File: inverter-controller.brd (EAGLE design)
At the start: 66 x 27.6 mm, 187 parts, among them IC1 STM32F334C8T6, IC2 SY7152ABC, IC3 LMV358MMX, IC4 LMV358MMX, IC5 SY7152ABC, J1 621006245821, J2 61300211121, K1 FINDER_34.51.7.024.0010FINDER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, K2 FINDER_34.51.7.024.0010FINDER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, K3 FINDER_34.51.7.024.0010FINDER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, U1 DIODES_AP3015KTR-G1DIODES_AP3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, X1 0289-9066**15EDGVC-3.81-02P-14, X2 0289-9066**15EDGVC-3.81-02P-14, X3 0289-9066**15EDGVC-3.81-02P-14, X4 0289-9066**15EDGVC-3.81-02P-14, X5 1365-10, X6 1365-16, X7 1365-10, X8 1365-10, Y1 NX2016SA-32M

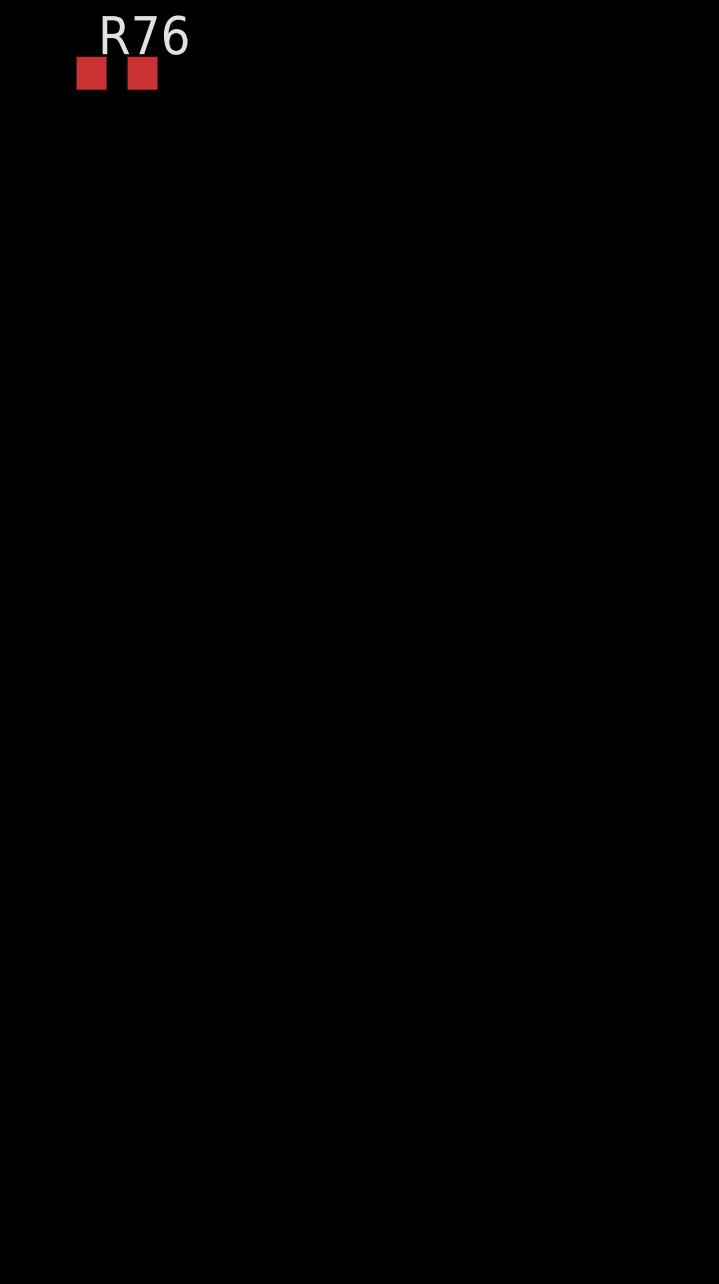
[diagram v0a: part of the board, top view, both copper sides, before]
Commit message: Relay soketleri eklendi.
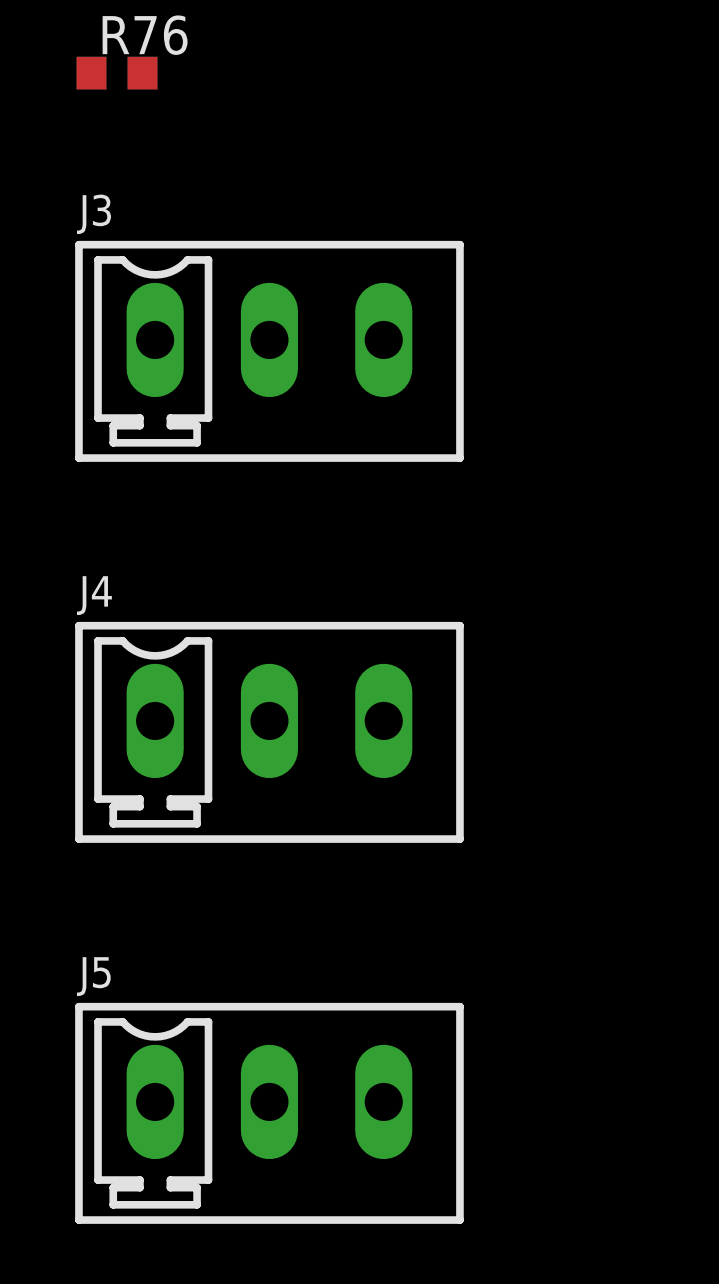
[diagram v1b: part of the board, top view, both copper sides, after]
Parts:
- added J3, J4, J5: MCV3, con-phoenix-381:MCV3
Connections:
- new net NC: J3.2, J4.2, J5.2
- new net NO: J3.3, J4.3, J5.3
- net COM1: now also J3.1
- net COM2: now also J4.1
- net COM3: now also J5.1
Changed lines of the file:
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@@
 <attribute name="VALUE" x="-126.365" y="-53.975" size="1.27" layer="27"/>
+</element>
+<element name="J3" library="con-phoenix-381" library_urn="urn:adsk.eagle:library:27486877" package="MCV3" package3d_urn="urn:adsk.eagle:package:27487037/1" value="MCV3" x="-120.65" y="-60.96" smashed="yes">
+<attribute name="NAME" x="-127" y="-57.15" size="1.016" layer="25" ratio="18"/>
+<attribute name="VALUE" x="-127" y="-66.929" size="0.8128" layer="27" ratio="10"/>
+</element>
+<element name="J4" library="con-phoenix-381" library_urn="urn:adsk.eagle:library:27486877" package="MCV3" package3d_urn="urn:adsk.eagle:package:27487037/1" value="MCV3" x="-120.65" y="-73.66" smashed="yes">
+<attribute name="NAME" x="-127" y="-69.85" size="1.016" layer="25" ratio="18"/>
+<attribute name="VALUE" x="-127" y="-79.629" size="0.8128" layer="27" ratio="10"/>
+</element>
+<element name="J5" library="con-phoenix-381" library_urn="urn:adsk.eagle:library:27486877" package="MCV3" package3d_urn="urn:adsk.eagle:package:27487037/1" value="MCV3" x="-120.65" y="-86.36" smashed="yes">
+<attribute name="NAME" x="-127" y="-82.55" size="1.016" layer="25" ratio="18"/>
+<attribute name="VALUE" x="-127" y="-92.329" size="0.8128" layer="27" ratio="10"/>
 </element>
 </elements>
@@
 <signal name="COM1">
 <contactref element="K1" pad="11"/>
+<contactref element="J3" pad="1"/>
+<wire x1="57.9" y1="60.89" x2="-124.46" y2="-60.96" width="0" layer="19" extent="1-1"/>
 </signal>
 <signal name="NO2">
@@
 <signal name="COM2">
 <contactref element="K2" pad="11"/>
+<contactref element="J4" pad="1"/>
+<wire x1="57.9" y1="50.73" x2="-124.46" y2="-73.66" width="0" layer="19" extent="1-1"/>
 </signal>
 <signal name="COM3">
 <contactref element="K3" pad="11"/>
+<contactref element="J5" pad="1"/>
+<wire x1="57.9" y1="40.57" x2="-124.46" y2="-86.36" width="0" layer="19" extent="1-1"/>
 </signal>
 <signal name="NO3">
@@
 <wire x1="18.76" y1="37.672" x2="-105.41" y2="-36.42" width="0" layer="19" extent="1-16"/>
 </signal>
+<signal name="NC">
+<contactref element="J3" pad="2"/>
+<contactref element="J4" pad="2"/>
+<contactref element="J5" pad="2"/>
+<wire x1="-120.65" y1="-73.66" x2="-120.65" y2="-86.36" width="0" layer="19" extent="1-1"/>
+<wire x1="-120.65" y1="-60.96" x2="-120.65" y2="-73.66" width="0" layer="19" extent="1-1"/>
+</signal>
+<signal name="NO">
+<contactref element="J3" pad="3"/>
+<contactref element="J4" pad="3"/>
+<contactref element="J5" pad="3"/>
+<wire x1="-116.84" y1="-73.66" x2="-116.84" y2="-86.36" width="0" layer="19" extent="1-1"/>
+<wire x1="-116.84" y1="-60.96" x2="-116.84" y2="-73.66" width="0" layer="19" extent="1-1"/>
+</signal>
 </signals>

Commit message: Mekanik kistaslar belirlendi.
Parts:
- removed D7: (no value), diode:SOD80C
- removed J5: MCV3, con-phoenix-381:MCV3
- removed K3: FINDER_34.51.7.024.0010FINDER_34.51.7.024.0010_0_0, Finder - 34.51.7.024.0010:FINDER_34.51.7.024.0010_0
- removed LED3: (no value), adafruit:CHIPLED_0805
- removed Q3: (no value), adafruit:SOT23
- removed R40: (no value), rcl:R0603
- removed R41: 22R, rcl:R0603
- removed R44: 470R, rcl:R0603
- moved J4 217.1 mm to (54.7, 54.2), turned to 180 degrees
- moved J3 203.2 mm to (62.4, 27.2)
- moved X6 169.9 mm to (54.5, 40.9)
- moved X2 146.7 mm to (51.2, 27.2), turned to 180 degrees
- moved X4 127.0 mm to (32.8, 27.2), turned to 180 degrees
- moved C4 112.1 mm to (27.9, 38.3), flipped to the bottom, turned to 90 degrees
- moved C5 102.3 mm to (29.1, 38.3), flipped to the bottom, turned to 90 degrees
- moved C3 100.7 mm to (29.0, 35.1), flipped to the bottom, turned to 270 degrees
- moved X3 93.5 mm to (42.0, 27.2), turned to 180 degrees
- moved X1 77.3 mm to (23.6, 27.2), turned to 180 degrees
- moved K1 20.0 mm to (33.7, 49.3)
- moved J1 19.6 mm to (45.7, 36.9)
- moved IC1 19.6 mm to (35.5, 36.9)
- moved K2 18.3 mm to (33.6, 55.7)
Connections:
- removed net COM3: J5.1, K3.11
- removed net N$28: Q3.1, R40.2, R41.1
- removed net N$31: D7.A, K3.A1, LED3.C, Q3.3
- removed net N$33: LED3.A, R44.1
- removed net NC3: K3.12
- removed net NO3: K3.14
- net GND: no longer Q3.2, R40.1
- net NC: no longer J5.2
- net NO: no longer J5.3
- net RELAY3: no longer R41.2
- net VDD: no longer D7.C, K3.A2, R44.2
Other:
- board size 66 x 27.6 mm -> 52 x 37.6 mm

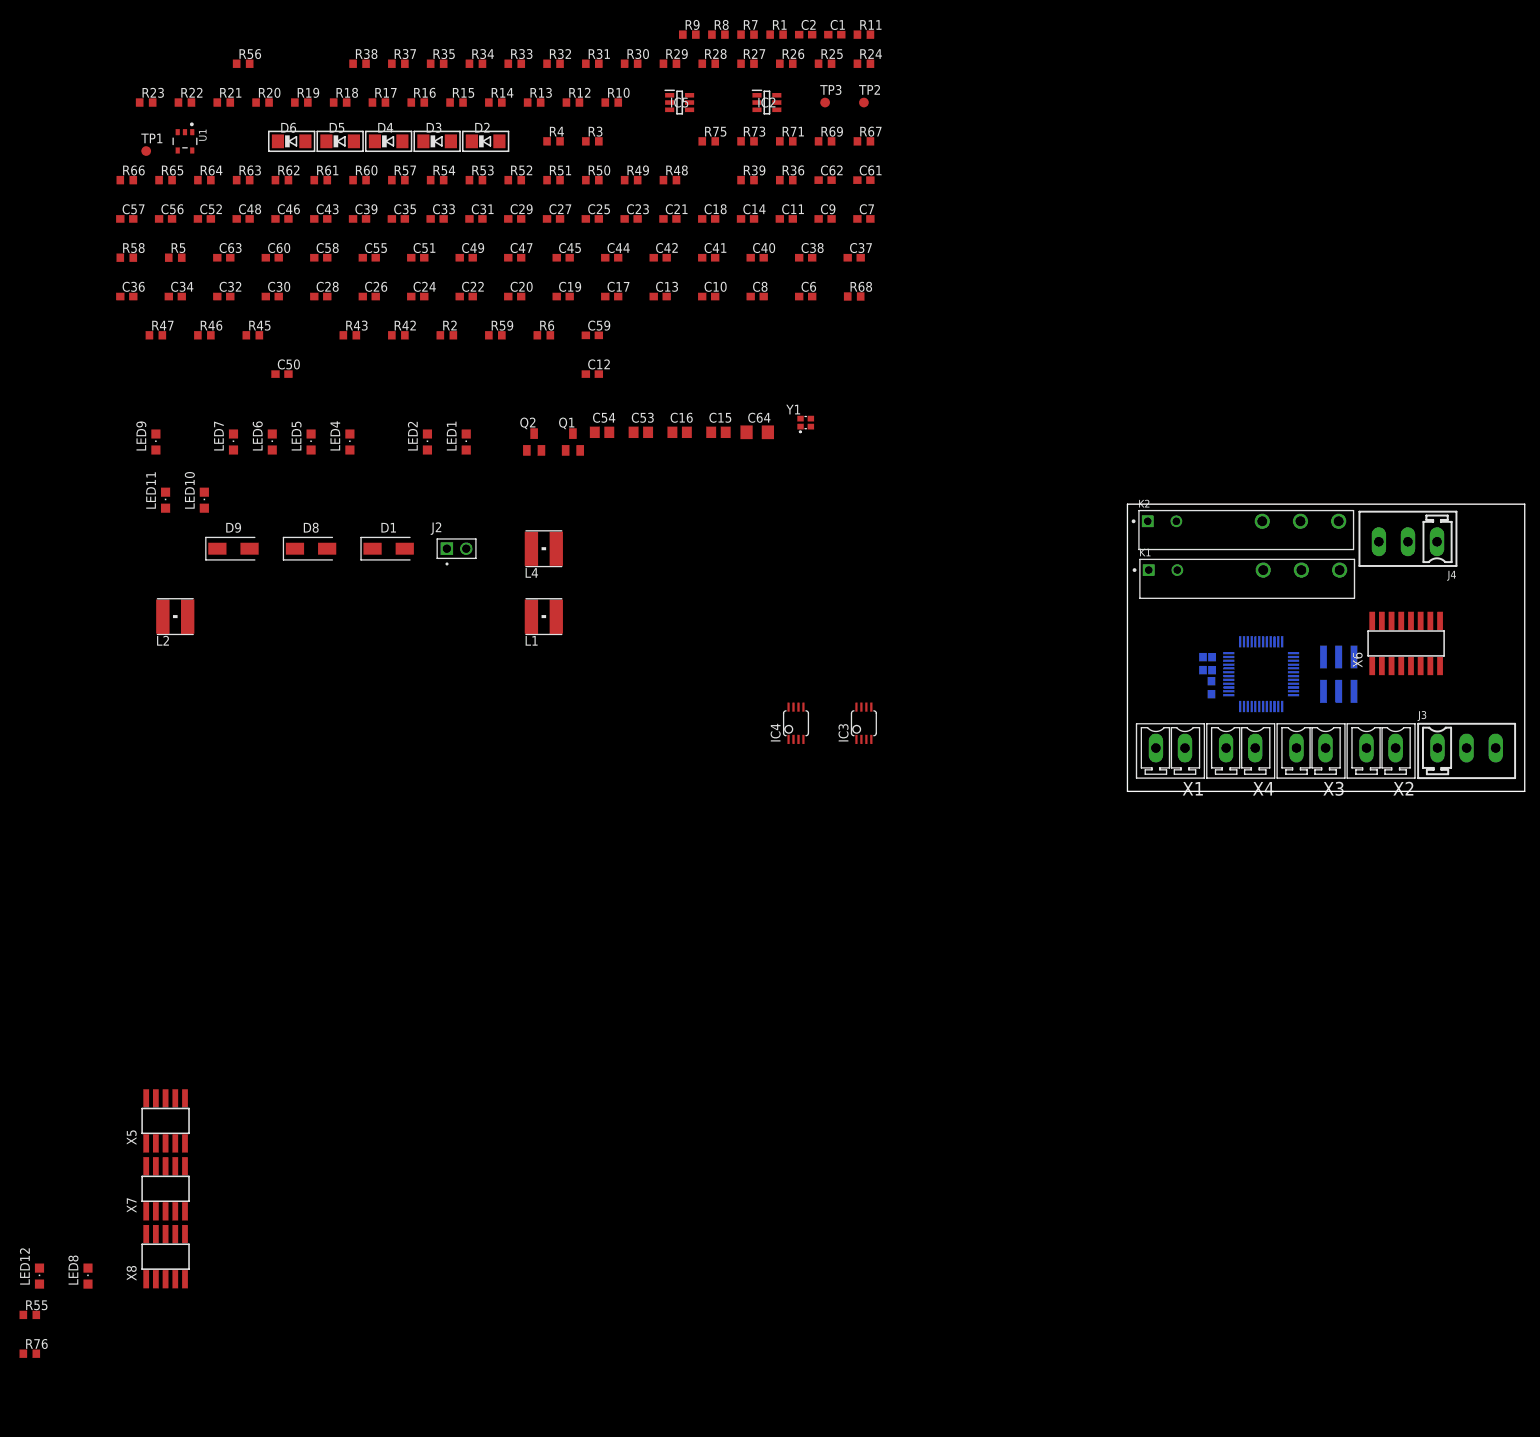
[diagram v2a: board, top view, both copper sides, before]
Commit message: Mini kart tasarimi icin sadelestirildi.
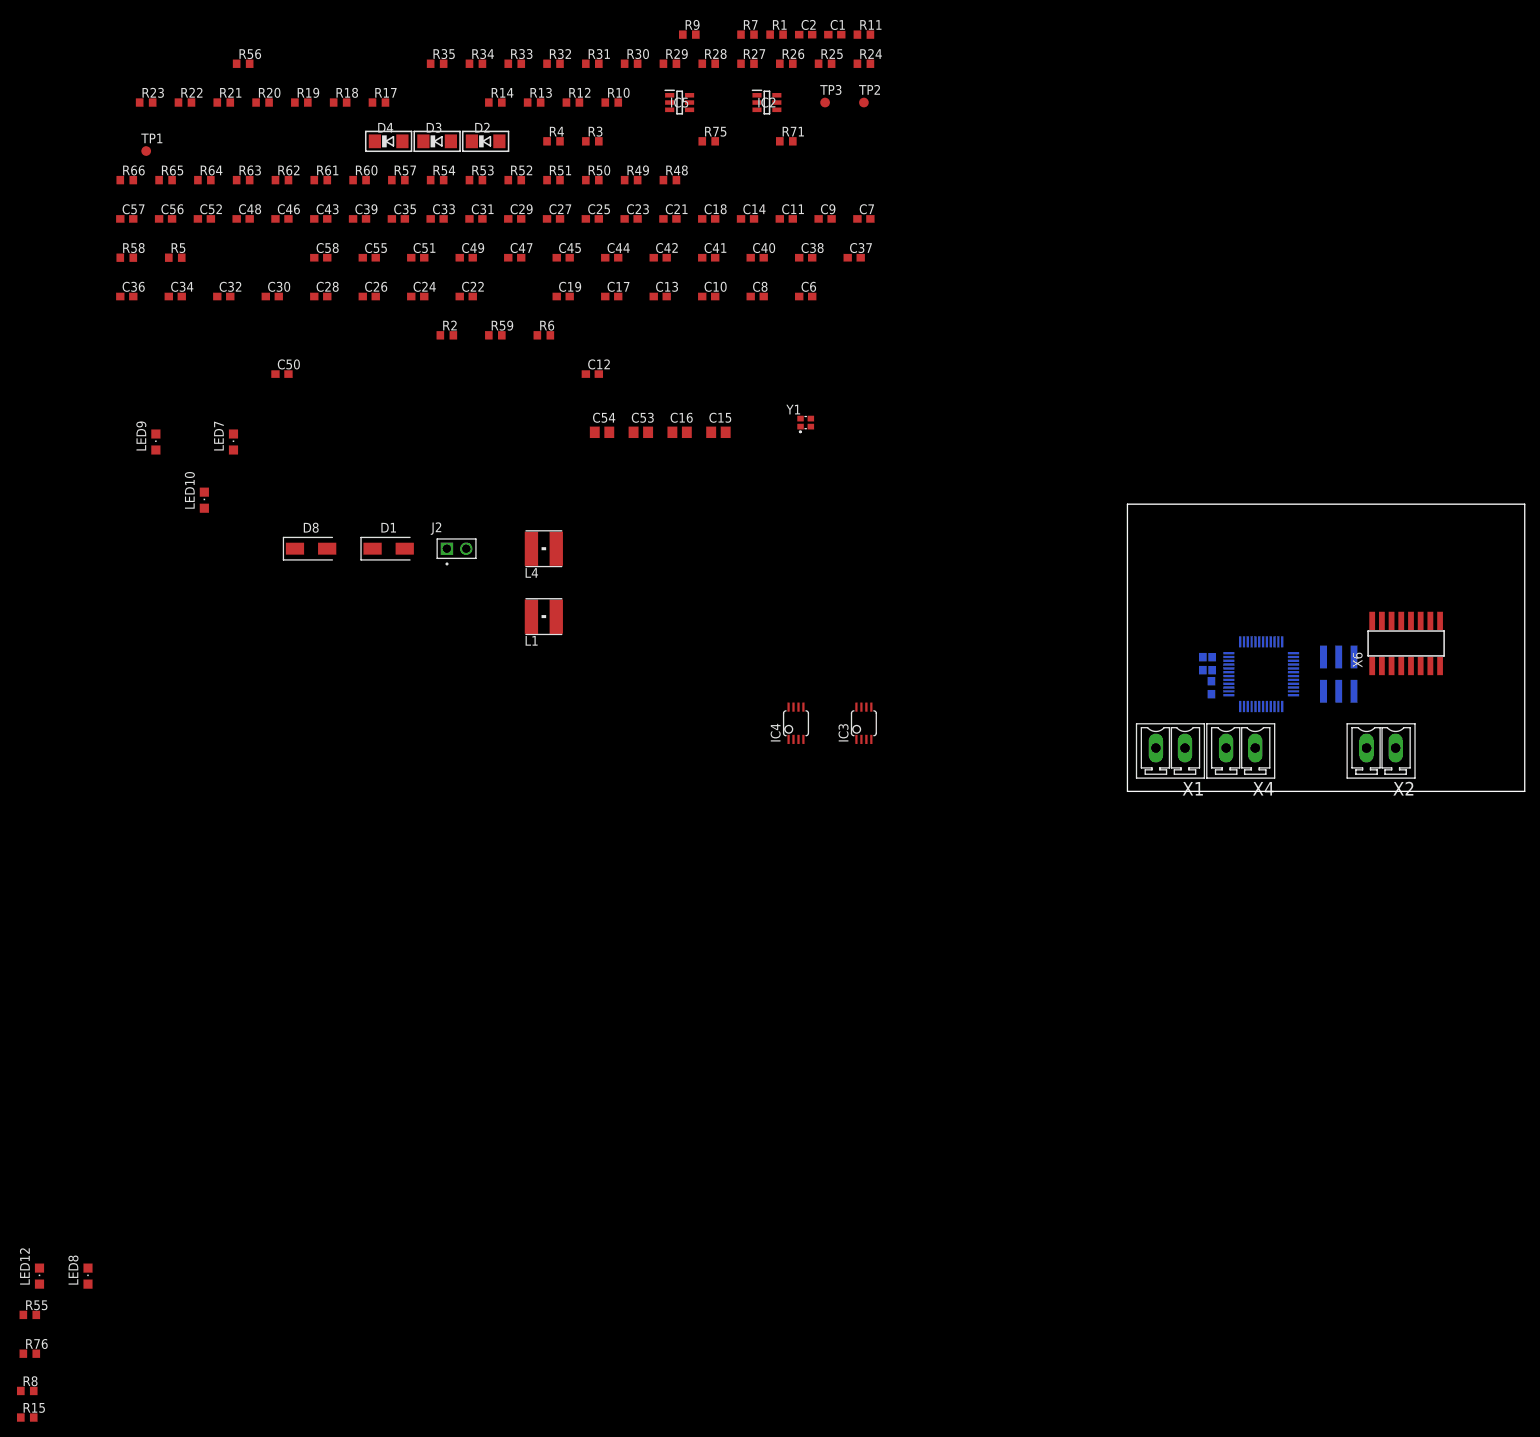
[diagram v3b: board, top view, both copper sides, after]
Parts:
- removed C20, C60, C63: 100n, rcl:C0603
- removed C59: 1019-3366**CAP 0603 CER 10uF 16V %20 X5R, rcl:C0603
- removed C61: 10n, rcl:C0603
- removed C62: 1n, rcl:C0603
- removed C64: 1u, rcl:C1206
- removed D5, D6: (no value), diode:SOD80C
- removed D9: 1119-3055, Diode:DIOM5226X290N
- removed J3, J4: MCV3, con-phoenix-381:MCV3
- removed K1, K2: FINDER_34.51.7.024.0010FINDER_34.51.7.024.0010_0_0, Finder - 34.51.7.024.0010:FINDER_34.51.7.024.0010_0
- removed L2: 1319-4102**INDUCTOR POWER 22UH 4X4X1.8MM SMD, wuerth-elektronik:WE-PD2_S
- removed LED1, LED11, LED2, LED4, LED5, LED6: (no value), adafruit:CHIPLED_0805
- removed Q1, Q2: (no value), adafruit:SOT23
- removed R16, R37, R38: (no value), rcl:R0603
- removed R36, R39: 22R, rcl:R0603
- removed R42, R43: 470R, rcl:R0603
- removed R45, R46, R47: 100R, rcl:R0603
- removed R67: 2M, rcl:R0603
- removed R68: 130K, rcl:R0603
- removed R69: 1k, rcl:R0603
- removed R73: NC, rcl:R0603
- removed U1: DIODES_AP3015KTR-G1DIODES_AP3015KTR-G1_0_0, AP3015KTR-G1:DIODES_AP3015KTR-G1_0
- removed X3: 0289-9066**15EDGVC-3.81-02P-14, con-phoenix-381_l:MCV2
- removed X5, X7, X8: 1365-10, con-leotronics:1365-10
- R56: value (none) -> 220R
- moved R8 199.3 mm to (-126.1, -57.0)
- moved R15 181.1 mm to (-126.1, -60.4)
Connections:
- removed net CAN_RX: IC1.45, X5.7, X5.8
- removed net CAN_TX: IC1.46, X5.5, X5.6
- removed net COM1: J3.1, K1.11
- removed net COM2: J4.1, K2.11
- removed net N$22: LED2.A, R43.1
- removed net N$24: Q1.1, R36.1, R37.2
- removed net N$25: Q2.1, R38.2, R39.1
- removed net N$26: LED5.A, R46.1
- removed net N$27: LED1.A, R42.1
- removed net N$29: D5.A, K1.A1, LED1.C, Q1.3
- removed net N$30: D6.A, K2.A1, LED2.C, Q2.3
- removed net N$32: LED6.A, R47.1
- removed net N$37: LED4.A, R45.1
- removed net N$44: D9.2, L2.2, U1.1
- removed net N$45: R67.1, R68.2, U1.3
- removed net N$49: LED11.A, R69.1
- removed net N$50: C59.1, C60.1, C61.1, L2.1, R73.2, U1.5
- removed net NC: J3.2, J4.2
- removed net NC1: K1.12
- removed net NC2: K2.12
- removed net NO: J3.3, J4.3
- removed net NO1: K1.14
- removed net NO2: K2.14
- removed net RELAY1: IC1.21, R36.2
- removed net RELAY2: IC1.22, R39.2
- removed net SPI1_CS: IC1.38, X8.10, X8.9
- removed net SPI1_MISO: IC1.40, X8.5, X8.6
- removed net SPI1_MOSI: IC1.41, X8.3, X8.4
- removed net USART1_RX: IC1.43, X7.7, X7.8
- removed net USART1_TX: IC1.42, X7.5, X7.6
- removed net VDD: C62.1, C63.1, C64.1, D5.C, D6.C, D9.1, K1.A2, K2.A2, R42.2, R43.2, R67.2, R69.2
- net +3V3: now also X6.1; no longer R73.1, X3.1, X5.1, X5.2, X6.2, X7.1, X7.2, X8.1
- net DGND: now also X6.2; no longer X5.10, X5.3, X5.4, X5.9, X6.1, X7.3, X7.4, X8.2
- net DRV1_EN: now also X6.10; no longer X6.9
- net DRV2_EN: now also X6.4; no longer X6.3
- net G11_PWM: now also X6.14; no longer X6.13
- net G12_PWM: now also X6.12; no longer X6.11
- net G13_PWM: now also X6.8; no longer X6.7
- net G14_PWM: now also X6.6; no longer X6.5
- net GND: no longer C20.2, C59.2, C60.2, C61.2, C62.2, C63.2, C64.2, LED11.C, LED4.C, LED5.C, LED6.C, Q1.2, Q2.2, R37.1, R38.1, R68.1, R8.1, U1.2
- net IA_SENS: now also X6.7; no longer X6.8
- net IB_SENS: now also X6.3; no longer X6.4
- net IIN_SENS: now also R8.1, X6.16; no longer R16.2, X6.15
- net I_IN: now also R8.2; no longer R16.1
- net N$13: no longer R45.2
- net N$14: no longer R46.2
- net N$20: no longer R47.2
- net NTC2: no longer C20.1, R8.2, X3.2
- net RELAY_EN: no longer IC1.37, U1.4
- net SPI1_SCK: no longer IC1.39, X8.7, X8.8
- net USART1_DIR: no longer X7.10, X7.9
- net VA_SENS: now also X6.9; no longer X6.10
- net VB_SENS: now also X6.5; no longer X6.6
- net VIN_2: now also R15.2; no longer R15.1
- net VIN_SENS: now also R15.1, X6.15; no longer R15.2, X6.16
- net VIN_SENS_DIFF: now also X6.13; no longer X6.14
- net VOUT_SENS_DIFF: now also X6.11; no longer X6.12

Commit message: DXF yuklendi
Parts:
- moved R8 161.6 mm to (11.0, 28.7), turned to 270 degrees
- moved R56 142.3 mm to (13.9, 28.7), turned to 90 degrees
- moved C36 135.3 mm to (9.30, 28.7), turned to 90 degrees
- moved LED9 130.6 mm to (15.4, 28.4), turned to 180 degrees
- moved C35 109.0 mm to (7.79, 28.7), turned to 90 degrees
- moved X6 45.0 mm to (9.56, 38.0), flipped to the bottom, turned to 90 degrees
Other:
- board size 52 x 37.6 mm -> 18.5 x 86.8 mm
